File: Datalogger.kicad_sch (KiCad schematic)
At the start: 0 parts

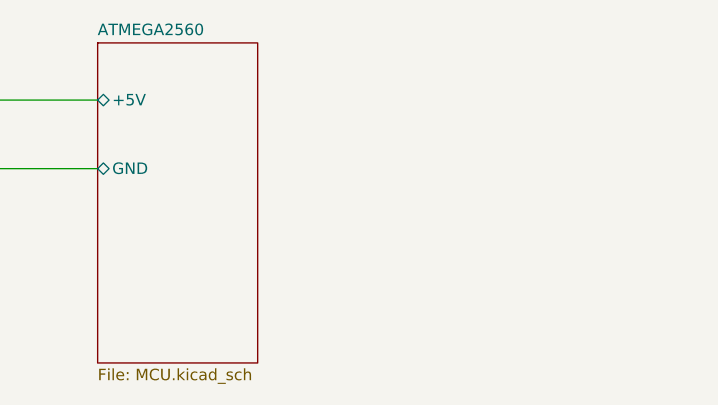
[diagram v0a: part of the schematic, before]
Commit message: "Resolved the issue of SS34 diode footprint. Problem was the pin on the downloaded footprint were not numbered
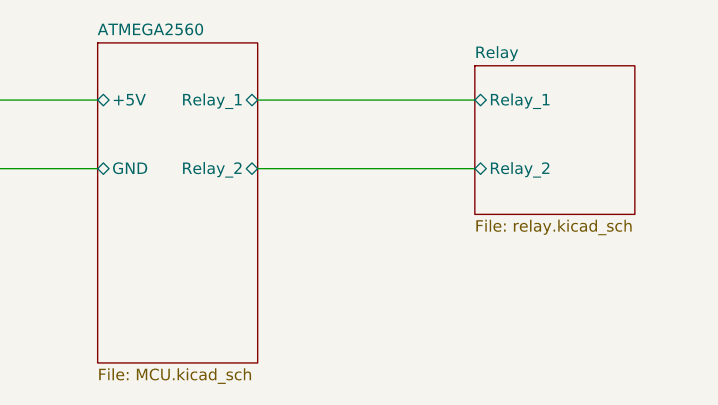
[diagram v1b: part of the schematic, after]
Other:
- added sheet Relay (relay.kicad_sch)
- sheet ATMEGA2560 ports: added Relay_1, Relay_2; removed none
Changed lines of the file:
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@@
 (kicad_sch (version 20230121) (generator eeschema)
   (paper "A4")
+  (wire (pts (xy 146.05 101.6) (xy 170.18 101.6))
+    (stroke (width 0) (type default))
+  )
   (wire (pts (xy 110.49 101.6) (xy 128.27 101.6))
+    (stroke (width 0) (type default))
+  )
+  (wire (pts (xy 146.05 93.98) (xy 170.18 93.98))
     (stroke (width 0) (type default))
   )
   (wire (pts (xy 110.49 93.98) (xy 128.27 93.98))
     (stroke (width 0) (type default))
+  )
+  (sheet (at 170.18 90.17) (size 17.78 16.51) (fields_autoplaced)
+    (stroke (width 0.1524) (type solid))
+    (fill (color 0 0 0 0.0000))
+    (property "Sheetname" "Relay" (at 170.18 89.4584 0)
+      (effects (font (size 1.27 1.27)) (justify left bottom))
+    )
+    (property "Sheetfile" "relay.kicad_sch" (at 170.18 107.2646 0)
+      (effects (font (size 1.27 1.27)) (justify left top))
+    )
+    (pin "Relay_1" bidirectional (at 170.18 93.98 180)
+      (effects (font (size 1.27 1.27)) (justify left))
+    )
+    (pin "Relay_2" bidirectional (at 170.18 101.6 180)
+      (effects (font (size 1.27 1.27)) (justify left))
+    )
+    (instances
+      (project "Datalogger"
+        (path "/9962467c-5981-4f6d-a8e0-b5534b13e1af" (page "4"))
+      )
+    )
   )
   (sheet (at 87.63 88.9) (size 22.86 17.78) (fields_autoplaced)
@@
       (effects (font (size 1.27 1.27)) (justify left))
     )
+    (pin "Relay_1" bidirectional (at 146.05 93.98 0)
+      (effects (font (size 1.27 1.27)) (justify right))
+    )
+    (pin "Relay_2" bidirectional (at 146.05 101.6 0)
+      (effects (font (size 1.27 1.27)) (justify right))
+    )
     (instances

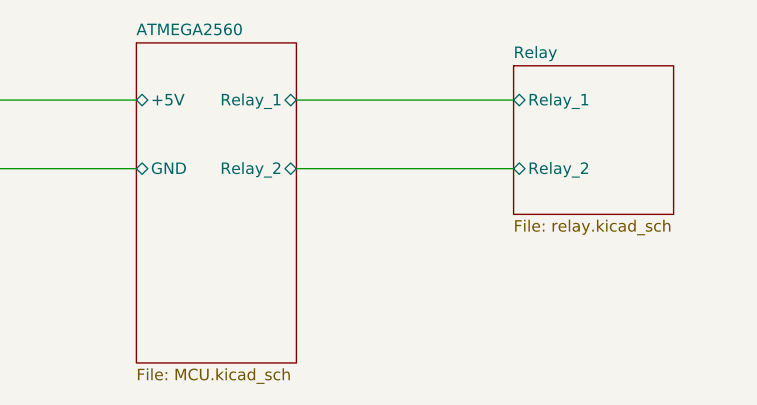
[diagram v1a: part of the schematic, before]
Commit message: Added DC motor driver
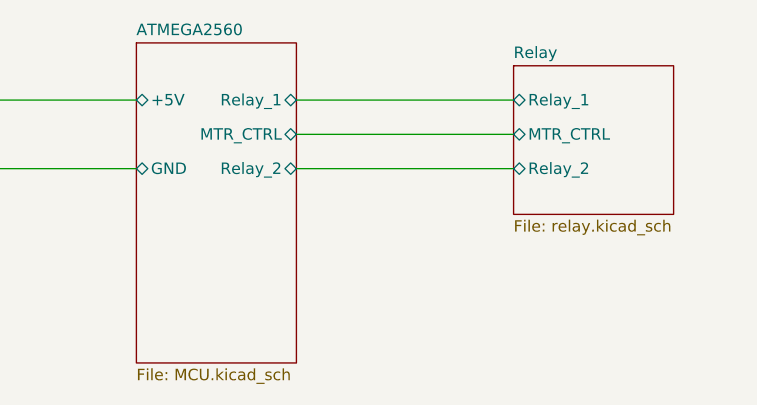
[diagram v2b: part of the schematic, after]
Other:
- sheet ATMEGA2560 ports: added MTR_CTRL; removed none
- sheet Relay ports: added MTR_CTRL; removed none
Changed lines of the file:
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@@
+    (stroke (width 0) (type default))
+  )
+  (wire (pts (xy 146.05 97.79) (xy 170.18 97.79))
     (stroke (width 0) (type default))
   )
@@
     )
     (pin "Relay_2" bidirectional (at 170.18 101.6 180)
+      (effects (font (size 1.27 1.27)) (justify left))
+    )
+    (pin "MTR_CTRL" bidirectional (at 170.18 97.79 180)
       (effects (font (size 1.27 1.27)) (justify left))
     )
@@
       (effects (font (size 1.27 1.27)) (justify right))
     )
+    (pin "MTR_CTRL" bidirectional (at 146.05 97.79 0)
+      (effects (font (size 1.27 1.27)) (justify right))
+    )

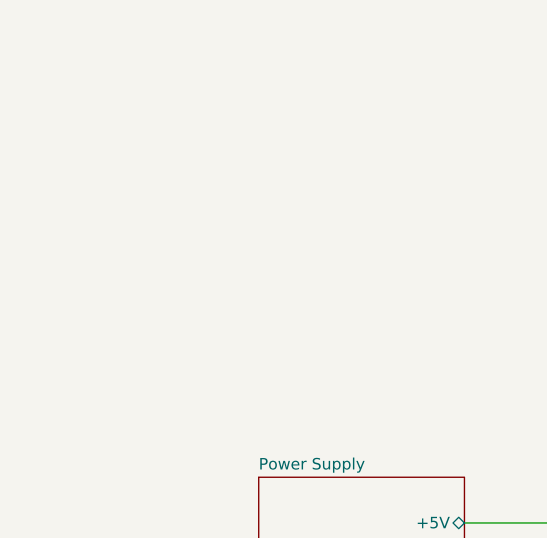
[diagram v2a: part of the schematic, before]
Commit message: Designed circuit for reading digital input. CHY74 (4 channel optocoupler) used
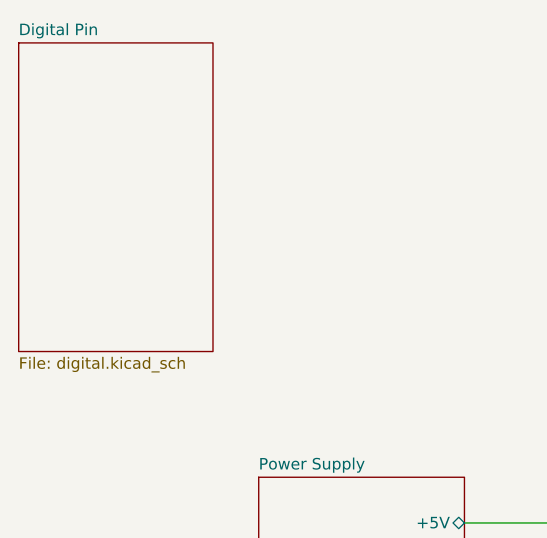
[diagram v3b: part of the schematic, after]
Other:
- added sheet Digital Pin (digital.kicad_sch)
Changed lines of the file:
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@@
+    )
+  )
+  (sheet (at 60.96 40.64) (size 21.59 34.29) (fields_autoplaced)
+    (stroke (width 0.1524) (type solid))
+    (fill (color 0 0 0 0.0000))
+    (property "Sheetname" "Digital Pin" (at 60.96 39.9284 0)
+      (effects (font (size 1.27 1.27)) (justify left bottom))
+    )
+    (property "Sheetfile" "digital.kicad_sch" (at 60.96 75.5146 0)
+      (effects (font (size 1.27 1.27)) (justify left top))
+    )
+    (property "Field2" "" (at 60.96 40.64 0)
+      (effects (font (size 1.27 1.27)) hide)
+    )
+    (instances
+      (project "Datalogger"
+        (path "/9962467c-5981-4f6d-a8e0-b5534b13e1af" (page "5"))
+      )
     )
   )

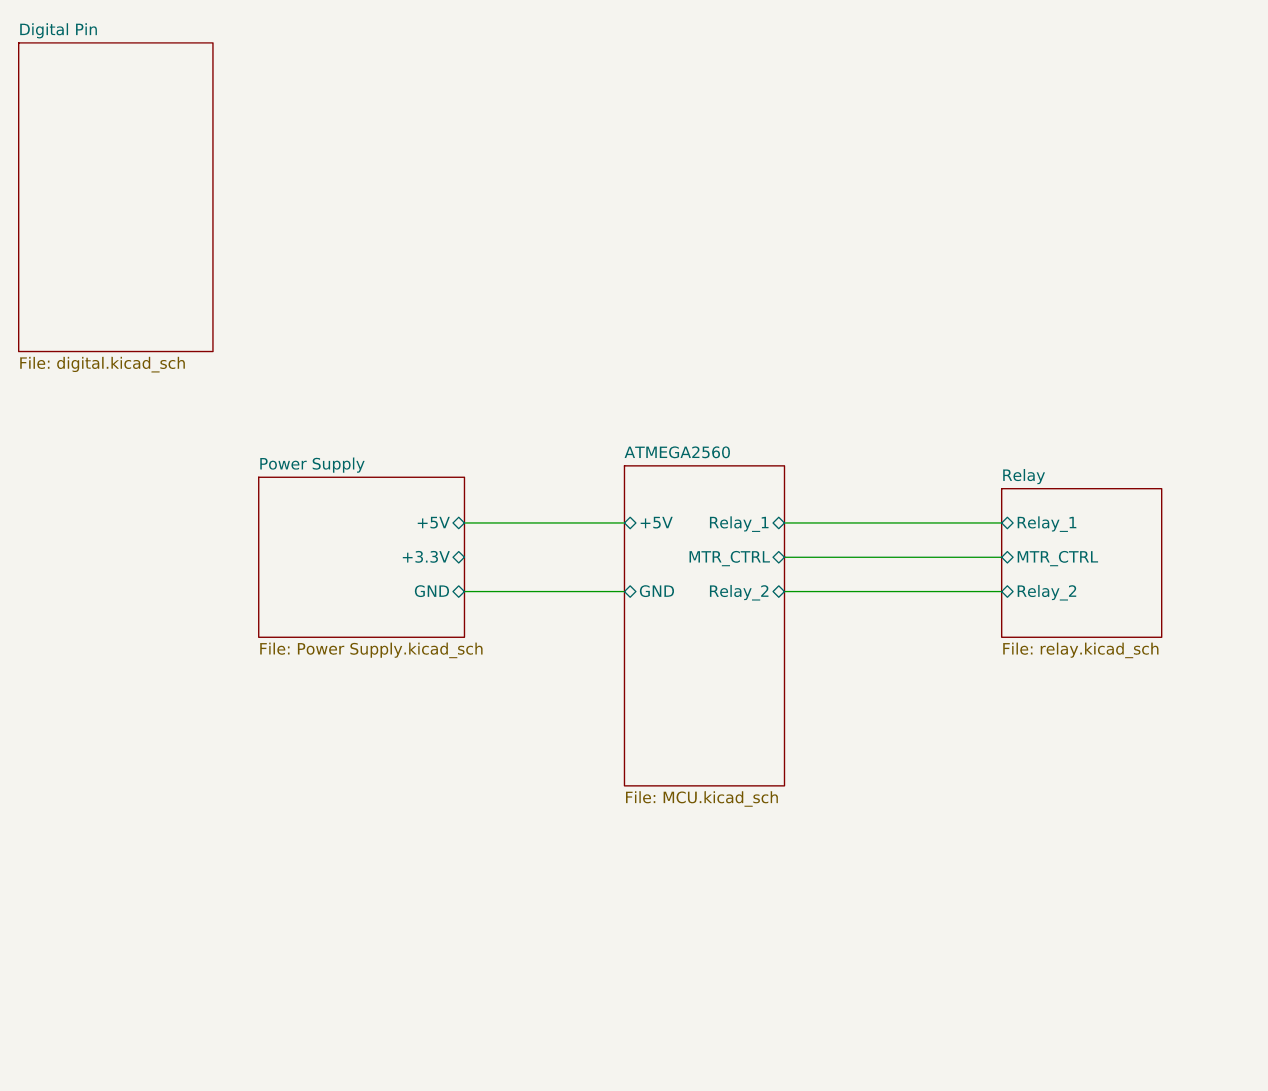
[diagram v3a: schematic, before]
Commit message: Analog input schematic
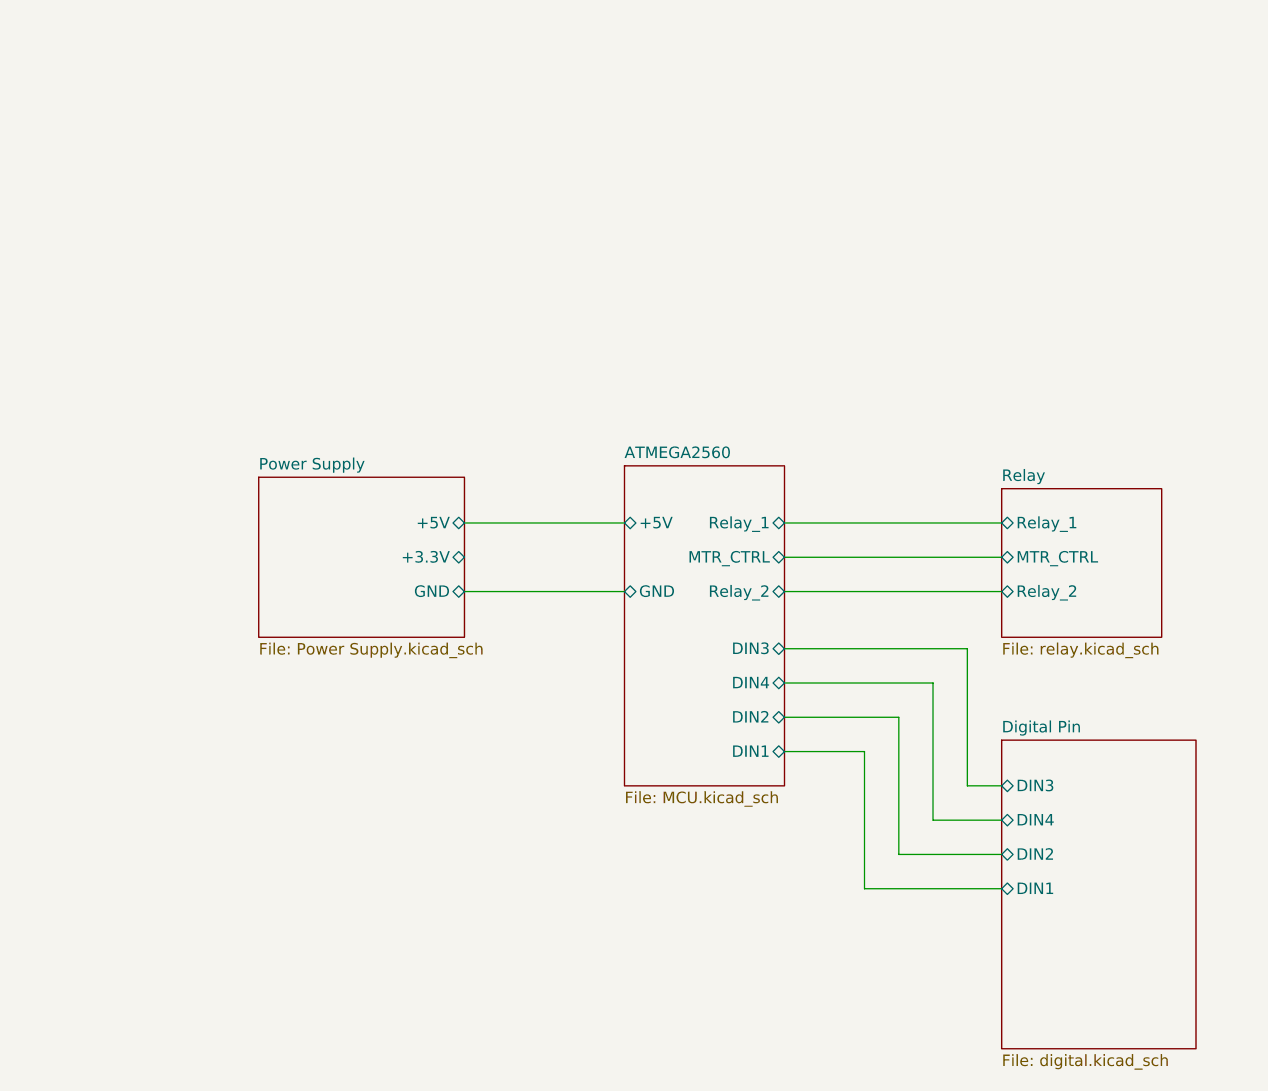
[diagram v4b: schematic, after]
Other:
- sheet ATMEGA2560 ports: added DIN1, DIN2, DIN3, DIN4; removed none
- sheet Digital Pin ports: added DIN1, DIN2, DIN3, DIN4; removed none
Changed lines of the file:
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@@
 (kicad_sch (version 20230121) (generator eeschema)
   (paper "A4")
+  (wire (pts (xy 154.94 134.62) (xy 170.18 134.62))
+    (stroke (width 0) (type default))
+  )
+  (wire (pts (xy 146.05 111.76) (xy 162.56 111.76))
+    (stroke (width 0) (type default))
+  )
   (wire (pts (xy 146.05 101.6) (xy 170.18 101.6))
     (stroke (width 0) (type default))
@@
     (stroke (width 0) (type default))
   )
+  (wire (pts (xy 146.05 119.38) (xy 154.94 119.38))
+    (stroke (width 0) (type default))
+  )
+  (wire (pts (xy 146.05 107.95) (xy 166.37 107.95))
+    (stroke (width 0) (type default))
+  )
   (wire (pts (xy 146.05 93.98) (xy 170.18 93.98))
+    (stroke (width 0) (type default))
+  )
+  (wire (pts (xy 158.75 130.81) (xy 170.18 130.81))
     (stroke (width 0) (type default))
   )
@@
     (stroke (width 0) (type default))
   )
+  (wire (pts (xy 154.94 119.38) (xy 154.94 134.62))
+    (stroke (width 0) (type default))
+  )
+  (wire (pts (xy 166.37 107.95) (xy 166.37 123.19))
+    (stroke (width 0) (type default))
+  )
+  (wire (pts (xy 166.37 123.19) (xy 170.18 123.19))
+    (stroke (width 0) (type default))
+  )
+  (wire (pts (xy 162.56 127) (xy 170.18 127))
+    (stroke (width 0) (type default))
+  )
   (wire (pts (xy 146.05 97.79) (xy 170.18 97.79))
+    (stroke (width 0) (type default))
+  )
+  (wire (pts (xy 158.75 115.57) (xy 158.75 130.81))
+    (stroke (width 0) (type default))
+  )
+  (wire (pts (xy 146.05 115.57) (xy 158.75 115.57))
+    (stroke (width 0) (type default))
+  )
+  (wire (pts (xy 162.56 111.76) (xy 162.56 127))
     (stroke (width 0) (type default))
   )
@@
     )
   )
-  (sheet (at 60.96 40.64) (size 21.59 34.29) (fields_autoplaced)
+  (sheet (at 170.18 118.11) (size 21.59 34.29) (fields_autoplaced)
     (stroke (width 0.1524) (type solid))
     (fill (color 0 0 0 0.0000))
-    (property "Sheetname" "Digital Pin" (at 60.96 39.9284 0)
+    (property "Sheetname" "Digital Pin" (at 170.18 117.3984 0)
       (effects (font (size 1.27 1.27)) (justify left bottom))
     )
-    (property "Sheetfile" "digital.kicad_sch" (at 60.96 75.5146 0)
+    (property "Sheetfile" "digital.kicad_sch" (at 170.18 152.9846 0)
       (effects (font (size 1.27 1.27)) (justify left top))
     )
-    (property "Field2" "" (at 60.96 40.64 0)
+    (property "Field2" "" (at 170.18 118.11 0)
       (effects (font (size 1.27 1.27)) hide)
+    )
+    (pin "DIN3" bidirectional (at 170.18 123.19 180)
+      (effects (font (size 1.27 1.27)) (justify left))
+    )
+    (pin "DIN4" bidirectional (at 170.18 127 180)
+      (effects (font (size 1.27 1.27)) (justify left))
+    )
+    (pin "DIN2" bidirectional (at 170.18 130.81 180)
+      (effects (font (size 1.27 1.27)) (justify left))
+    )
+    (pin "DIN1" bidirectional (at 170.18 134.62 180)
+      (effects (font (size 1.27 1.27)) (justify left))
     )
     (instances
@@
       (effects (font (size 1.27 1.27)) (justify right))
     )
+    (pin "DIN2" bidirectional (at 146.05 115.57 0)
+      (effects (font (size 1.27 1.27)) (justify right))
+    )
+    (pin "DIN4" bidirectional (at 146.05 111.76 0)
+      (effects (font (size 1.27 1.27)) (justify right))
+    )
+    (pin "DIN3" bidirectional (at 146.05 107.95 0)
+      (effects (font (size 1.27 1.27)) (justify right))
+    )
+    (pin "DIN1" bidirectional (at 146.05 119.38 0)
+      (effects (font (size 1.27 1.27)) (justify right))
+    )
